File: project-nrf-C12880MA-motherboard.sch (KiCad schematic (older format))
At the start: 4 parts, among them J1 Left, J2 Right

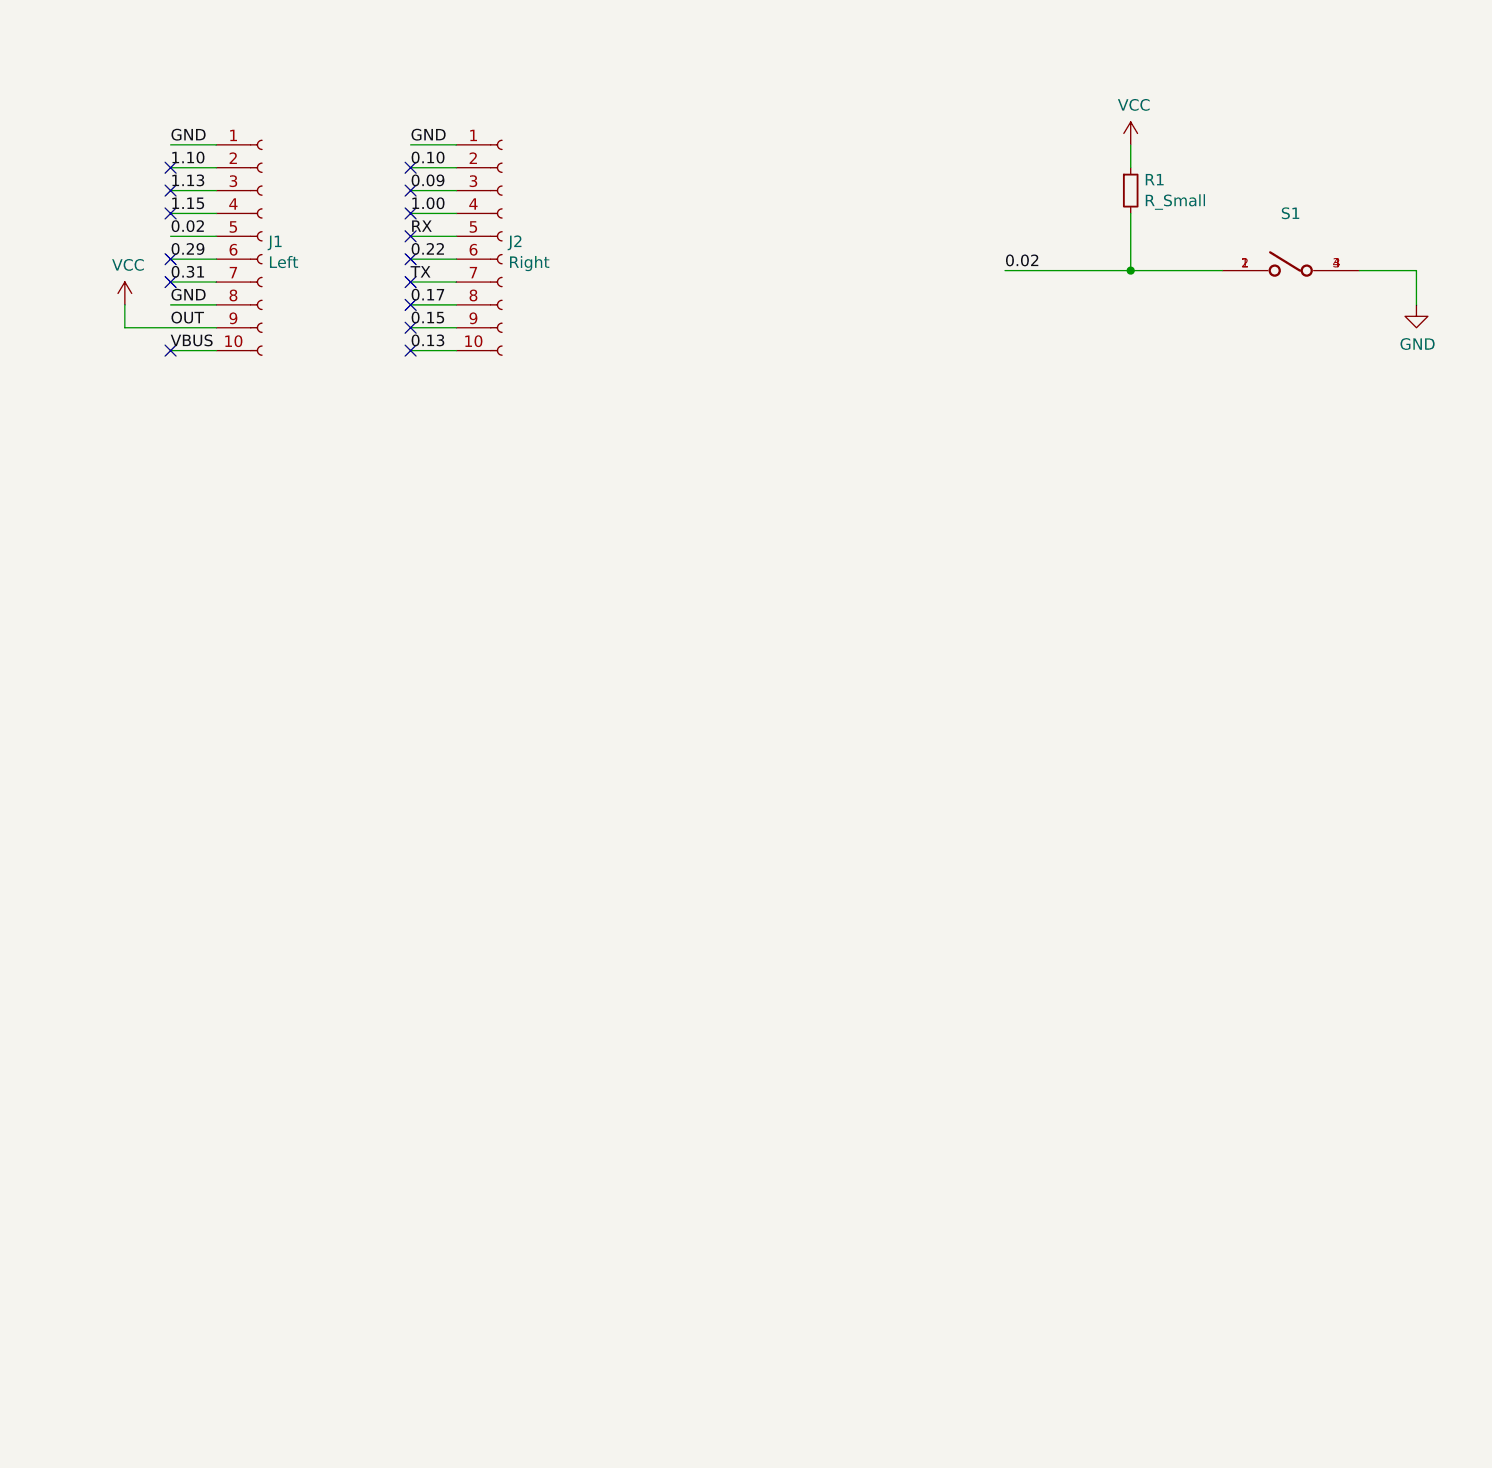
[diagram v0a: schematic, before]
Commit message: Setup power input, add most components
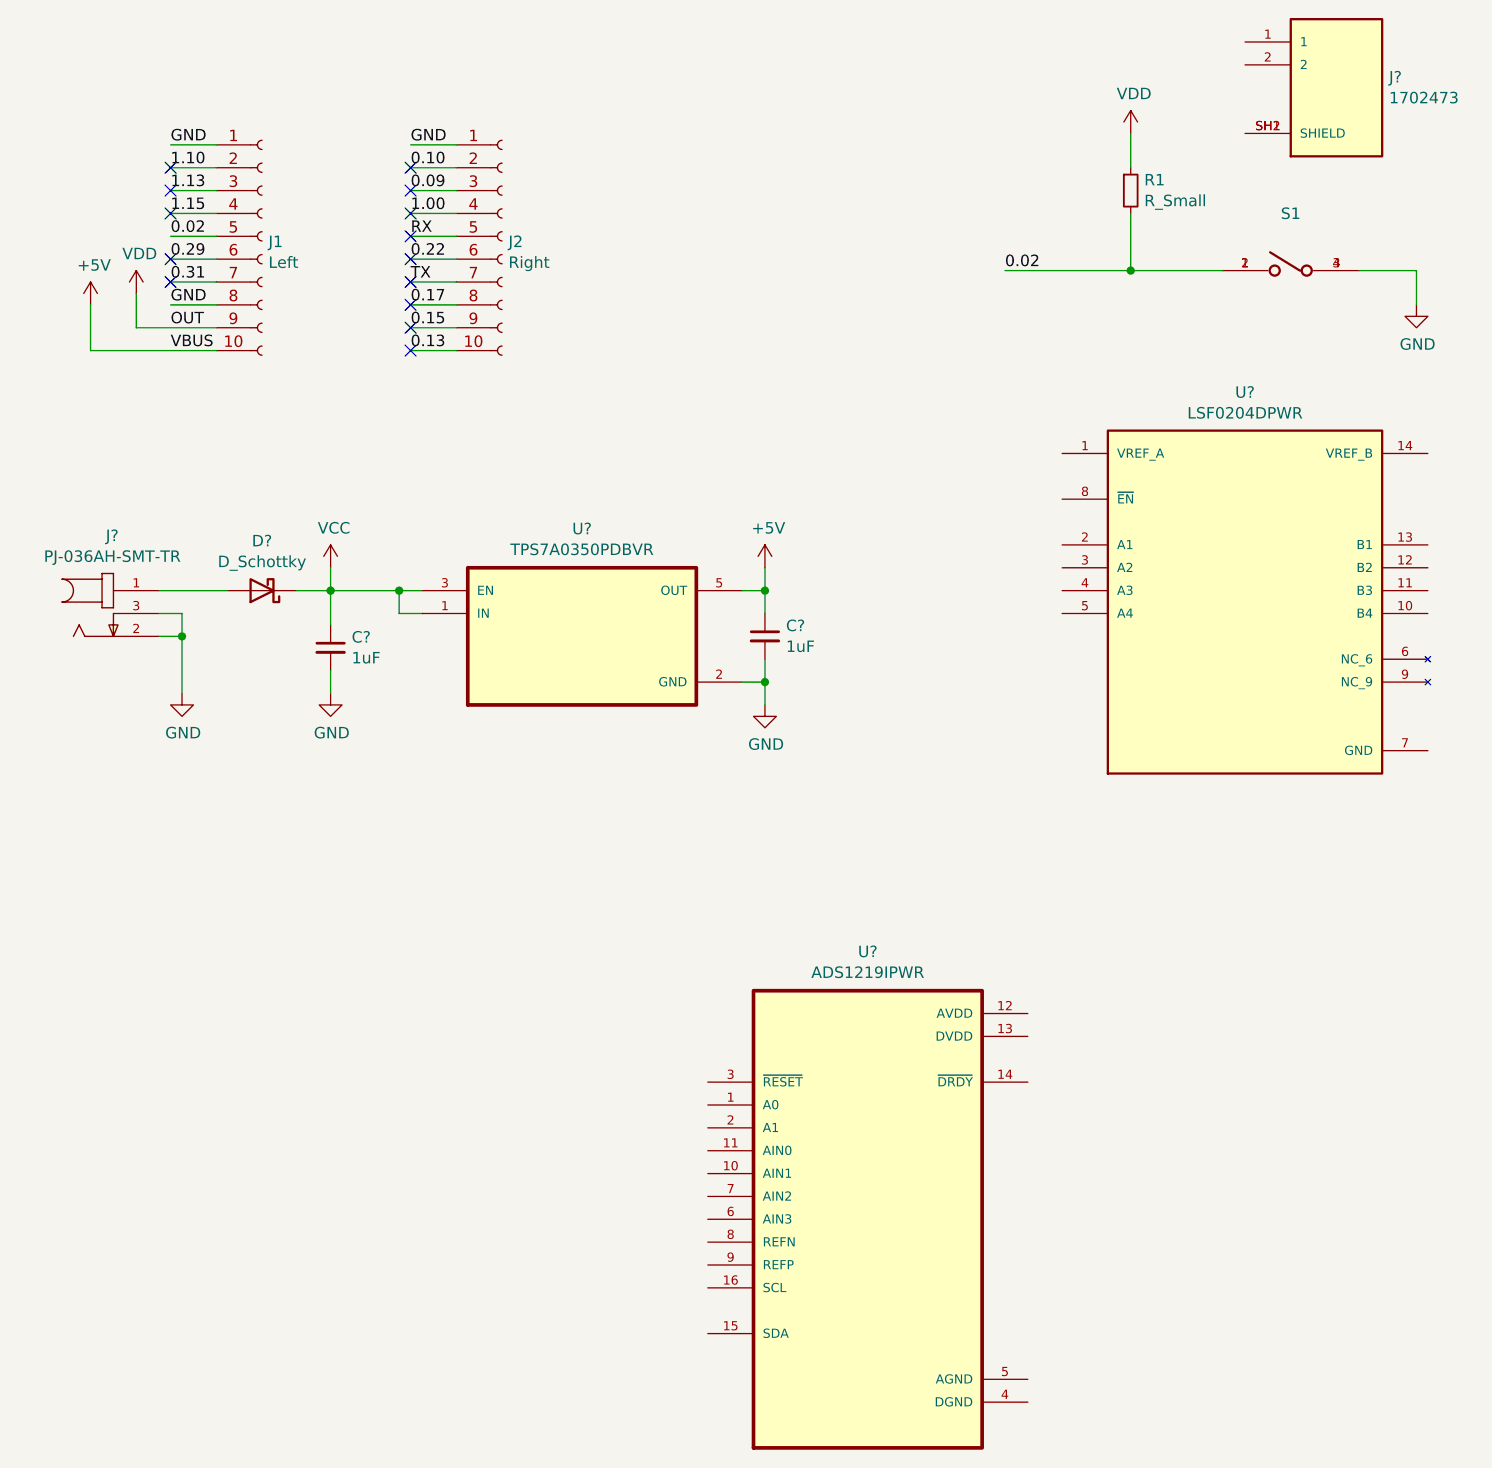
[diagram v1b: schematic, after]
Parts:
- added C? (x2): 1uF, Capacitor_SMD:C_0603_1608Metric, symbol Device:C_Small
- added D?: D_Schottky, CUS10S30,H3F:DIO_CUS520,H3F, symbol Device:D_Schottky
- added J?: PJ-036AH-SMT-TR, CUI_PJ-036AH-SMT-TR, symbol PJ-036AH-SMT-TR:PJ-036AH-SMT-TR
- added J?: 1702473, PHOENIX_1702473, symbol 1702473:1702473
- added U?: TPS7A0350PDBVR, SOT95P280X145-5N, symbol TPS7A0233PDBVR:TPS7A0233PDBVR
- added U?: ADS1219IPWR, SOP65P640X120-16N, symbol ADS1219IPWR:ADS1219IPWR
- added U?: LSF0204DPWR, SOP65P640X120-14N, symbol LSF0204DPWR:LSF0204DPWR
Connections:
- net GND: now also C?.2, C?.2, J?.2, J?.3, U?.2 (GND)
- net VCC: now also C?.1, D?.1 (K), U?.1 (IN), U?.3 (EN); no longer J1.9 (Pin_9), R1.1
- net VBUS renamed +5V
- net +5V: now also C?.1, U?.5 (OUT)
- new net: D?.2 (A), J?.1
- new net: J?.SH1 (SHIELD), J?.SH2 (SHIELD)
- new net VDD: J1.9 (Pin_9), R1.1
- no-connect marks 15 -> 14

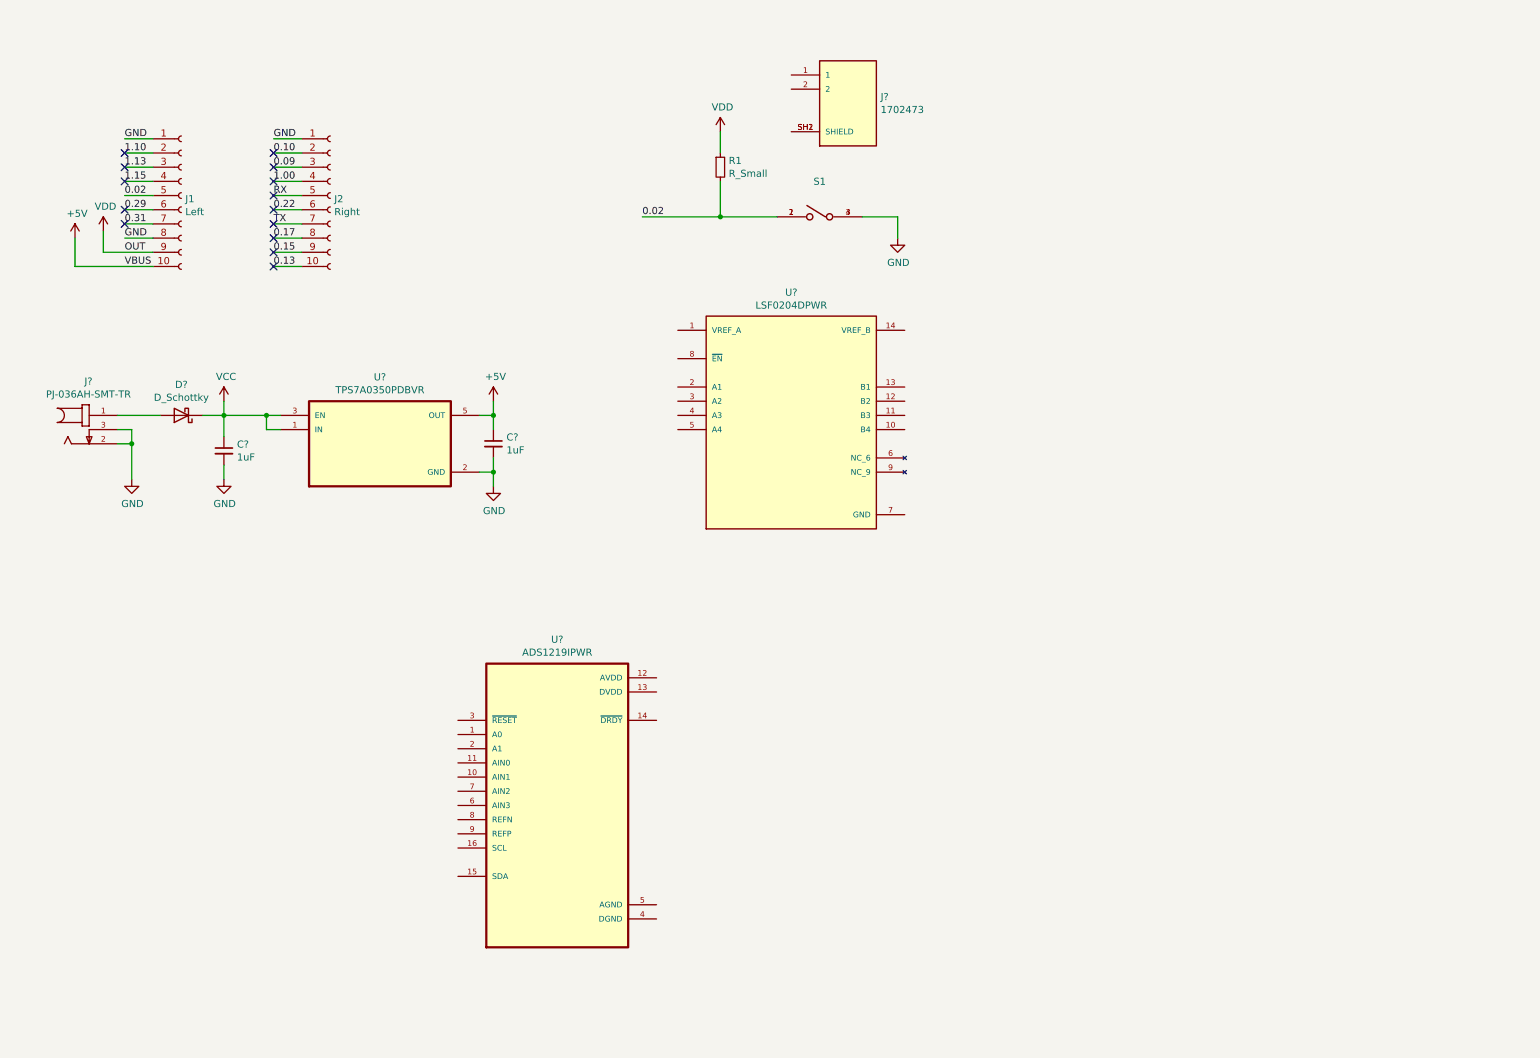
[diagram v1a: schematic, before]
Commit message: Schematic done
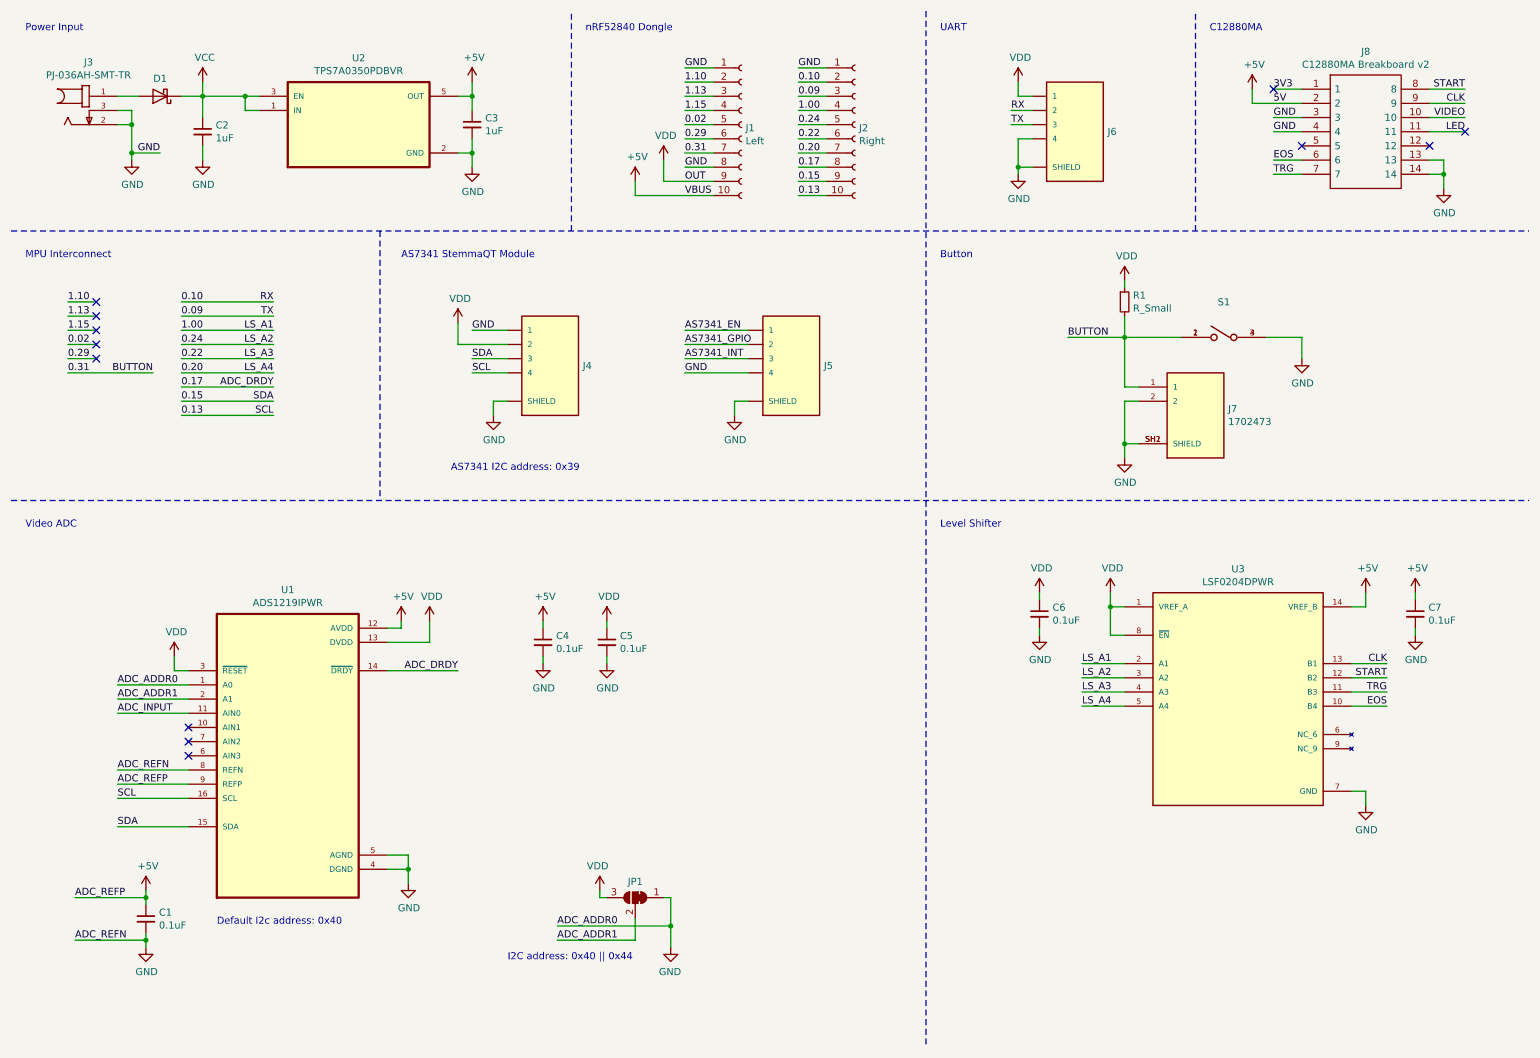
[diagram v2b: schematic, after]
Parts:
- added C1, C4, C5, C6, C7: 0.1uF, Capacitor_SMD:C_0603_1608Metric, symbol Device:C_Small
- added J4, J5, J6: SM04B-SRSS-TB(LF)(SN), JST_SM04B-SRSS-TB(LF)(SN), symbol SM04B-SRSS-TB_LF__SN_:SM04B-SRSS-TB(LF)(SN)
- added J8: C12880MA Breakboard v2, 15650122601000, symbol 15650122601000:15650122601000
- added JP1: SolderJumper_3_Bridged12, Jumper:SolderJumper-3_P1.3mm_Bridged12_RoundedPad1.0x1.5mm, symbol Jumper:SolderJumper_3_Bridged12
- gave numbers to parts that had none: 8
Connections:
- net RX is gone; now on net 0.24: J2.5 (Pin_5)
- net TX is gone; now on net 0.20: J2.7 (Pin_7)
- net +5V: now also U1.12 (AVDD), U1.9 (REFP), U3.14 (VREF_B), C1.1, C4.1, C7.1, J8.2
- net 0.02: no longer R1.2, S1.1, S1.2
- net 0.09: now also J6.3
- net 0.10: now also J6.2
- net 0.13: now also U1.16 (SCL), J4.4
- net 0.15: now also U1.15 (SDA), J4.3
- net 0.17: now also U1.14 (~DRDY)
- net 0.22: now also U3.4 (A3)
- net 0.31: now also J7.1, R1.2, S1.1, S1.2
- net 1.00: now also U3.2 (A1)
- net GND: now also J7.2, J7.SH1 (SHIELD), J7.SH2 (SHIELD), U1.1 (A0), U1.4 (DGND), U1.5 (AGND), U1.8 (REFN), U3.7 (GND), C1.2, C4.2, C5.2, C6.2, C7.2, J4.1, J4.S1 (SHIELD), J4.S2 (SHIELD), J5.4, J5.S1 (SHIELD), J5.S2 (SHIELD), J6.4, J6.S1 (SHIELD), J6.S2 (SHIELD), J8.13, J8.14, J8.3, J8.4, JP1.1 (A)
- net VDD: now also U1.13 (DVDD), U1.3 (~RESET), U3.1 (VREF_A), U3.8 (~EN), C5.1, C6.1, J4.2, J6.1, JP1.3 (B)
- net ADC_INPUT: now reaches U1.11 (AIN0)
- net ADC_ADDR1: now reaches U1.2 (A1)
- net ADC_ADDR1: now also JP1.2 (C)
- net EOS: now reaches U3.10 (B4)
- net EOS: now also J8.6
- net TRG: now reaches U3.11 (B3)
- net TRG: now also J8.7
- net START: now reaches U3.12 (B2)
- net START: now also J8.8
- net CLK: now reaches U3.13 (B1)
- net CLK: now also J8.9
- net 0.24: now reaches U3.3 (A2)
- net 0.20: now reaches U3.5 (A4)
- new net 3V3: J8.1
- new net AS7341_EN: J5.1
- new net AS7341_GPIO: J5.2
- new net AS7341_INT: J5.3
- new net LED: J8.11
- new net VIDEO: J8.10
- no-connect marks 14 -> 12
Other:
- note added: "AS7341 I2C address: 0x39"
- note added: "AS7341 StemmaQT Module"
- note added: "Button"
- note added: "C12880MA"
- note added: "Default I2c address: 0x40"
- note added: "I2C address: 0x40 || 0x44"
- note added: "Level Shifter"
- note added: "MPU Interconnect"
- note added: "Power Input"
- note added: "UART"
- note added: "Video ADC"
- note added: "nRF52840 Dongle"
- moved on the sheet: C2, C3, D1, J1, J2, J3, J7, R1, S1, U1, U2, U3

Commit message: Started routing
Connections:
- net ADC_INPUT is gone; now on net VIDEO: U1.11 (AIN0)
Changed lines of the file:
@@
 Wire Wire Line
 	1250 5450 1750 5450
-Text Label 1250 5450 0    50   ~ 0
-ADC_INPUT
 $Comp
 L power:VDD #PWR04
@@
 Text Notes 7050 4150 0    50   ~ 0
 Level Shifter
+Text Label 1250 5450 0    50   ~ 0
+VIDEO
 $EndSCHEMATC
